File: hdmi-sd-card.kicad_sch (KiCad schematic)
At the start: 33 parts, among them J4 HDMI-A_WE_685119134923, J5 MicroSD_693071020811, U10 TPD4E05U06QDQARQ1, U11 TPD4E05U06QDQARQ1, U12 TPD4E05U06QDQARQ1, U14 TPD4E05U06QDQARQ1

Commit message: [#65754] Rename project
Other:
- title: SO-DIMM DDR5 Tester -> RDIMM DDR5 Tester

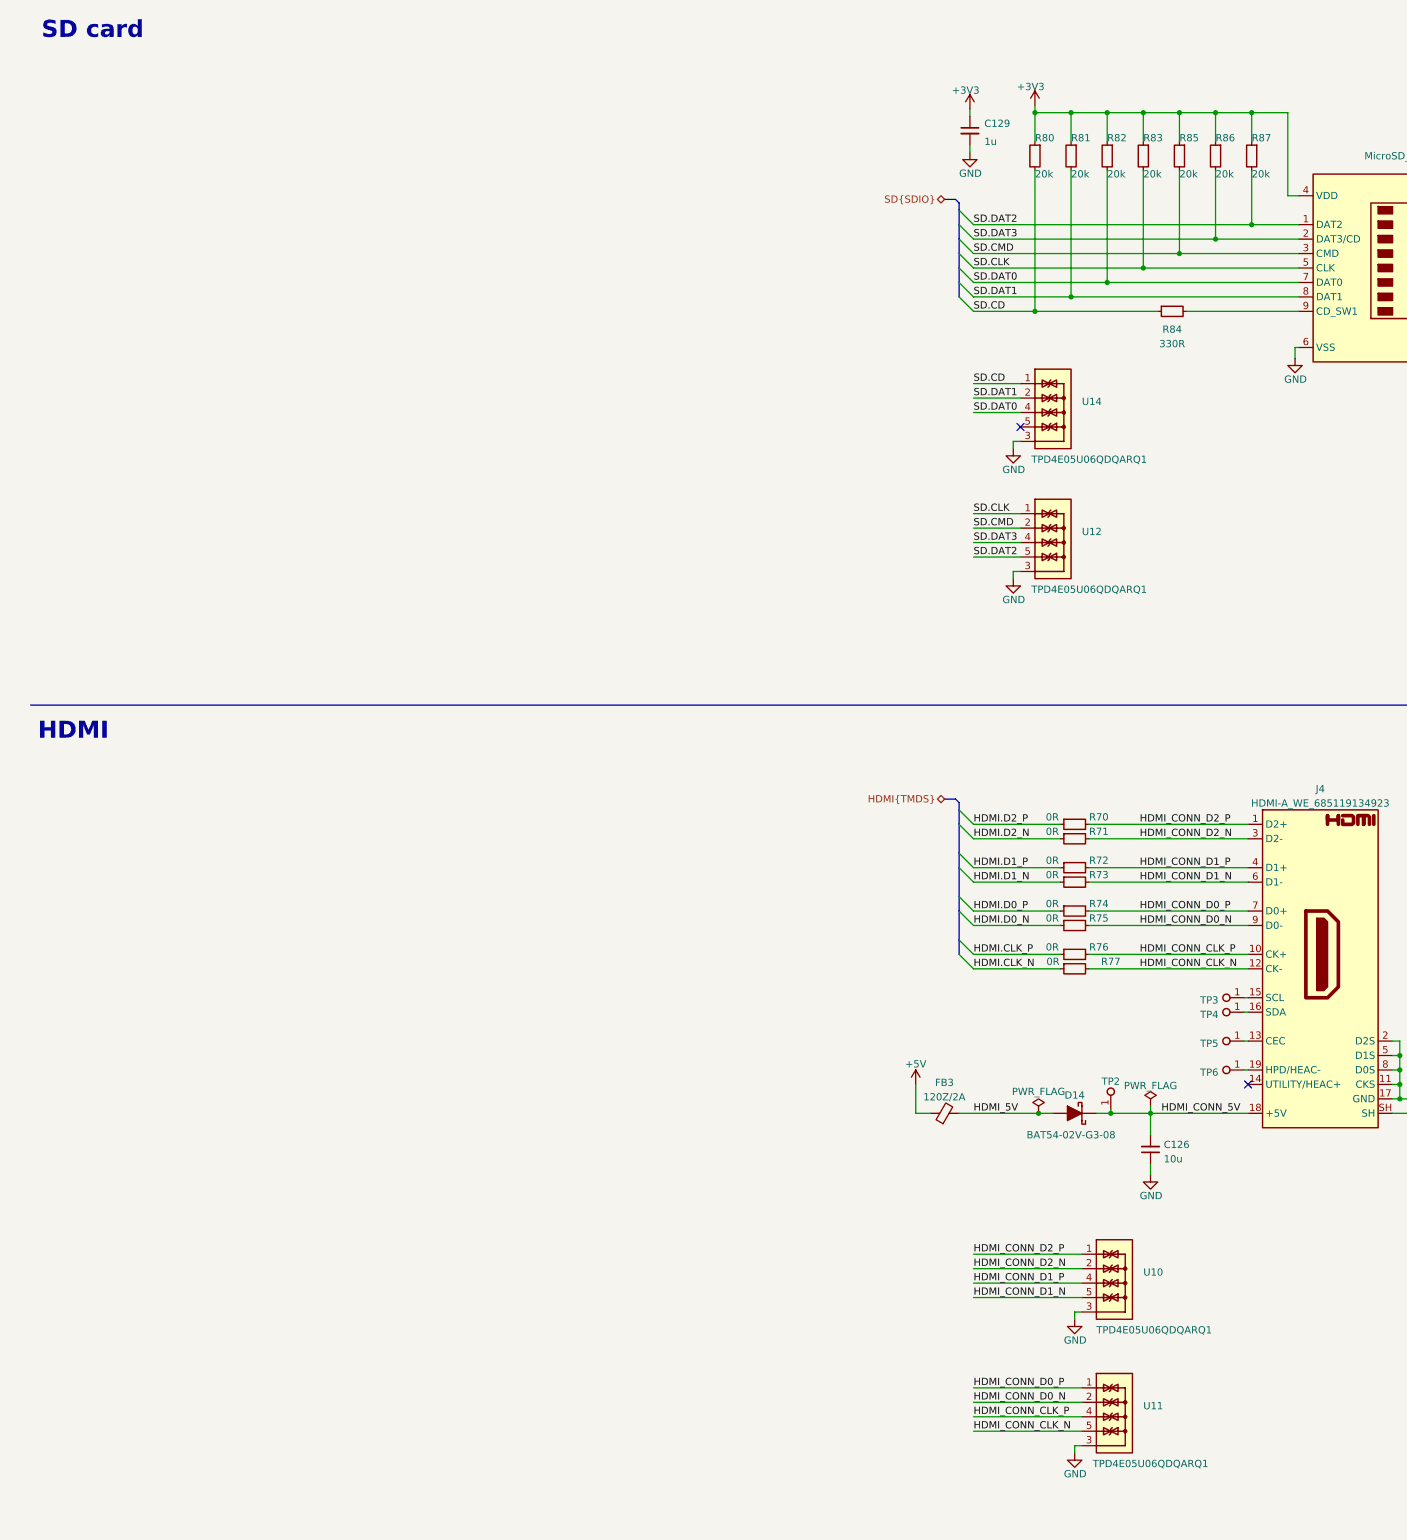
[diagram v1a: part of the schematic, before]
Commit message: [#66727] Finish connecting HDMI driver. Add SD card logic level converter. Add SD 3.0 support
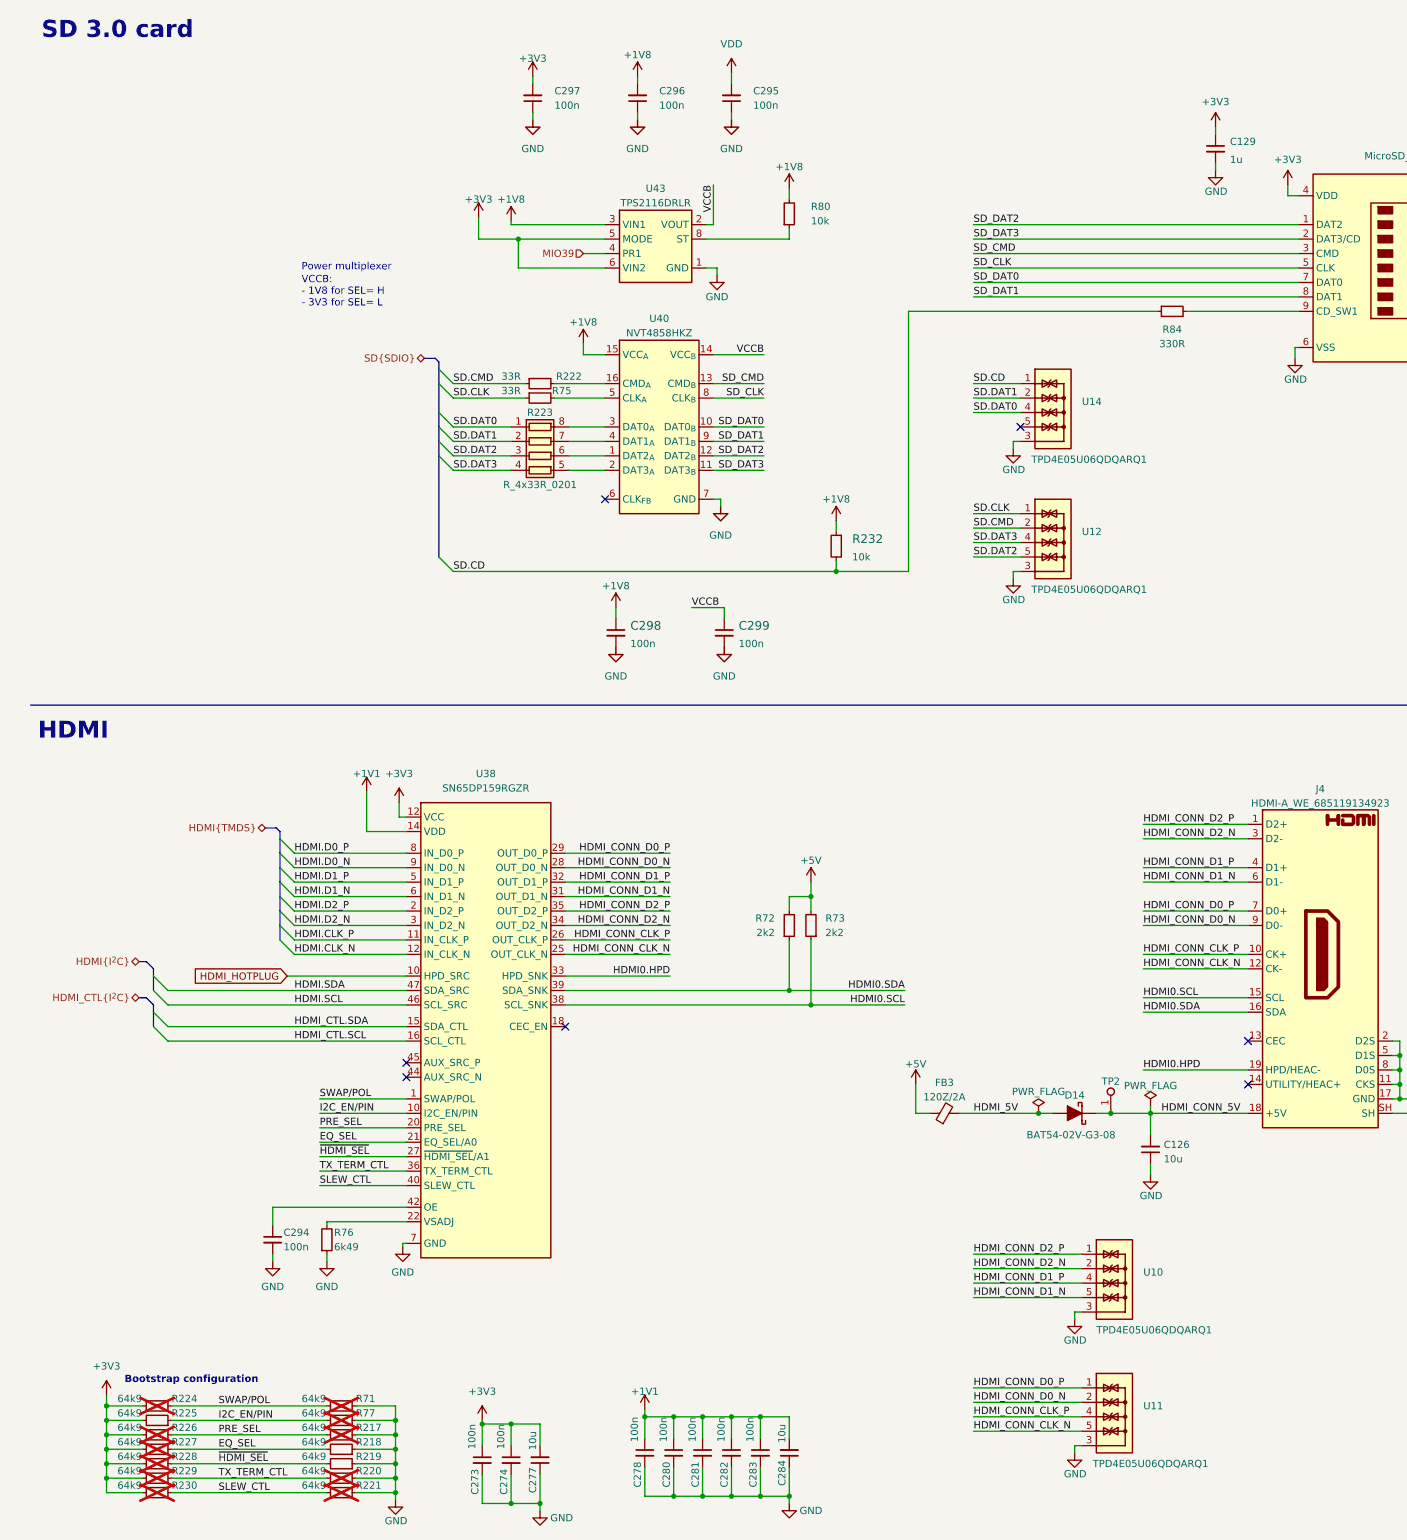
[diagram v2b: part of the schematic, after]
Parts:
- removed R70, R71, R72, R73, R74, R75, R76, R77: R_0R_0402, antmicro-footprints:R_0402_1005Metric, symbol antmicroResistors0402:R_0R_0402
- removed R80, R81, R82, R83, R85, R86, R87: R_20k_0402, antmicro-footprints:R_0402_1005Metric, symbol antmicroResistors0402:R_20k_0402
- removed TP3, TP4, TP5, TP6: TP_1mm_SMD, antmicro-footprints:TP_SMD_1mm, symbol antmicroTestPoints:TP_1mm_SMD
- added C273, C274, C278, C280, C281, C282, C283, C294, C295, C296, C297: C_100n_0402, antmicro-footprints:C_0402_1005Metric, symbol antmicroCapacitors0402:C_100n_0402
- added C277, C284: C_10u_10V_0402, antmicro-footprints:C_0402_1005Metric, symbol antmicroCapacitors0402:C_10u_10V_0402
- added C298, C299: C_100n_0402, kria-k26-devboard-footprints:C_0402_1005Metric, symbol kria-k26-devboard:C_100n_0402
- added R217, R218, R219, R220, R221, R224, R225, R226, R227, R228, R229, R230, R71, R77: R_64k9_0402, antmicro-footprints:R_0402_1005Metric, symbol antmicroResistors0402:R_64k9_0402
- added R222, R75: R_33R_0402, antmicro-footprints:R_0402_1005Metric, symbol antmicroResistors0402:R_33R_0402
- added R223: R_4x33R_0201_array, antmicro-footprints:R_Array_4x0201_Panasonic_EXB18V, symbol antmicroResistorNetworksArrays:R_4x33R_0201_array
- added R232: R_10k_0402, kria-k26-devboard-footprints:R_0402_1005Metric, symbol kria-k26-devboard:R_10k_0402
- added R72, R73: R_2k2_0402, antmicro-footprints:R_0402_1005Metric, symbol antmicroResistors0402:R_2k2_0402
- added R76: R_6k49_0402, antmicro-footprints:R_0402_1005Metric, symbol antmicroResistors0402:R_6k49_0402
- added R80: R_10k_0402, antmicro-footprints:R_0402_1005Metric, symbol antmicroResistors0402:R_10k_0402
- added U38: SN65DP159RGZR, antmicro-footprints:VQFN-48_7x7mm_P0.5mm_EP4.1x4.1mm, symbol antmicroInterfaceDriversReceiversTransceivers:SN65DP159RGZR
- added U40: NVT4858_XQFN, antmicro-footprints:SOT1161-2, symbol antmicroLogicTranslatorsLevelShifters:NVT4858_XQFN
- added U43: TPS2116DRLR, antmicro-footprints:SOT-583, symbol antmicroPMICPowerDistributionSwitchesLoadDrivers:TPS2116DRLR
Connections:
- net +3V3: now also C273.1, C274.1, C277.2, C297.2, R224.2, R225.2, R226.2, R227.2, R228.2, R229.2, R230.2, U38.12 (VCC), U38.43 (VCC), U43.5 (MODE), U43.6 (VIN2)
- net +5V: now also R72.2, R73.2
- net GND: now also C273.2, C274.2, C277.1, C278.2, C280.2, C281.2, C282.2, C283.2, C284.1, C294.2, C295.1, C296.1, C297.1, C298.2, C299.2, R217.1, R218.1, R219.1, R220.1, R221.1, R71.1, R76.1, R77.1, U38.19 (GND), U38.30 (GND), U38.41 (GND), U38.49 (GND), U38.7 (GND), U40.7 (GND), U43.1 (GND)
- net HDMI.CLK_N: now also U38.12 (VCC)
- net HDMI.CLK_P: now also U38.11 (IN_CLK_P)
- net HDMI.D0_N: now also U38.9 (IN_D0_N)
- net HDMI.D0_P: now also U38.8 (IN_D0_P)
- net HDMI.D1_N: now also U38.6 (IN_D1_N)
- net HDMI.D1_P: now also U38.5 (IN_D1_P)
- net HDMI.D2_N: now also U38.3 (IN_D2_N)
- net HDMI.D2_P: now also U38.2 (IN_D2_P)
- net HDMI_CONN_CLK_N: now also U38.25 (OUT_CLK_N)
- net HDMI_CONN_CLK_P: now also U38.26 (OUT_CLK_P)
- net HDMI_CONN_D0_N: now also U38.28 (OUT_D0_N)
- net HDMI_CONN_D0_P: now also U38.29 (OUT_D0_P)
- net HDMI_CONN_D1_N: now also U38.31 (OUT_D1_N)
- net HDMI_CONN_D1_P: now also U38.32 (OUT_D1_P)
- net HDMI_CONN_D2_N: now also U38.34 (OUT_D2_N)
- net HDMI_CONN_D2_P: now also U38.35 (OUT_D2_P)
- net SD.CD: now also R232.2
- net SD.CLK: now also R75.1; no longer J5.5 (CLK)
- net SD.CMD: now also R222.1; no longer J5.3 (CMD)
- net SD.DAT0: now also R223.1 (R1.1); no longer J5.7 (DAT0)
- net SD.DAT1: now also R223.2 (R2.1); no longer J5.8 (DAT1)
- net SD.DAT2: now also R223.3 (R3.1); no longer J5.1 (DAT2)
- net SD.DAT3: now also R223.4 (R4.1); no longer J5.2 (DAT3/CD)
- net HDMI0.SCL: now reaches J4.15 (SCL)
- net HDMI0.SCL: now also R73.1, U38.38 (SCL_SNK)
- net HDMI0.SDA: now reaches J4.16 (SDA)
- net HDMI0.SDA: now also R72.1, U38.39 (SDA_SNK)
- net HDMI0.HPD: now reaches J4.19 (HPD/HEAC-)
- net HDMI0.HPD: now also U38.33 (HPD_SNK)
- new net: R76.2, U38.22 (VSADJ)
- new net: R223.6 (R3.2), U40.1 (DAT2_{A})
- new net: R222.2, U40.16 (CMD_{A})
- new net: R223.5 (R4.2), U40.2 (DAT3_{A})
- new net: R223.8 (R1.2), U40.3 (DAT0_{A})
- new net: R223.7 (R2.2), U40.4 (DAT1_{A})
- new net: R75.2, U40.5 (CLK_{A})
- new net: C294.1, U38.42 (OE)
- new net: R80.1, U43.8 (ST)
- new net +1V1: C278.1, C280.1, C281.1, C282.1, C283.1, C284.2, C295.2, U38.14 (VDD), U38.23 (VDD), U38.24 (VDD), U38.37 (VDD), U38.48 (VDD)
- new net +1V8: C296.2, C298.1, R232.1, R80.2, U40.15 (VCC_{A}), U43.3 (VIN1)
- new net EQ_SEL: R218.2, R227.1, U38.21 (EQ_SEL/A0)
- new net HDMI.SCL: U38.46 (SCL_SRC)
- new net HDMI.SDA: U38.47 (SDA_SRC)
- new net HDMI_CTL.SCL: U38.16 (SCL_CTL)
- new net HDMI_CTL.SDA: U38.15 (SDA_CTL)
- new net HDMI_HOTPLUG: U38.10 (I2C_EN/PIN)
- new net I2C_EN/PIN: R225.1, R77.2, U38.10 (I2C_EN/PIN)
- new net MIO39: U43.4 (PR1)
- new net PRE_SEL: R217.2, R226.1, U38.20 (PRE_SEL)
- new net SD_CLK: J5.5 (CLK), U40.8 (CLK_{B})
- new net SD_CMD: J5.3 (CMD), U40.13 (CMD_{B})
- new net SD_DAT0: J5.7 (DAT0), U40.10 (DAT0_{B})
- new net SD_DAT1: J5.8 (DAT1), U40.9 (DAT1_{B})
- new net SD_DAT2: J5.1 (DAT2), U40.12 (DAT2_{B})
- new net SD_DAT3: J5.2 (DAT3/CD), U40.11 (DAT3_{B})
- new net SLEW_CTL: R221.2, R230.1, U38.40 (SLEW_CTL)
- new net SWAP/POL: R224.1, R71.2, U38.1 (SWAP/POL)
- new net TX_TERM_CTL: R220.2, R229.1, U38.36 (TX_TERM_CTL)
- new net VCCB: C299.1, U40.14 (VCC_{B}), U43.2 (VOUT), U43.7 (VOUT)
- new net ~{HDMI_SEL}: R219.2, R228.1, U38.27 (~{HDMI_SEL}/A1)
- no-connect marks 2 -> 7
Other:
- note added: "Bootstrap configuration"
- note added: "Power multiplexer"
- note added: "SD 3.0 card"
- note added: "VCCB: - 1V8 for SEL= H - 3V3 for SEL= L"
- note removed: "SD card"
- moved on the sheet: C129

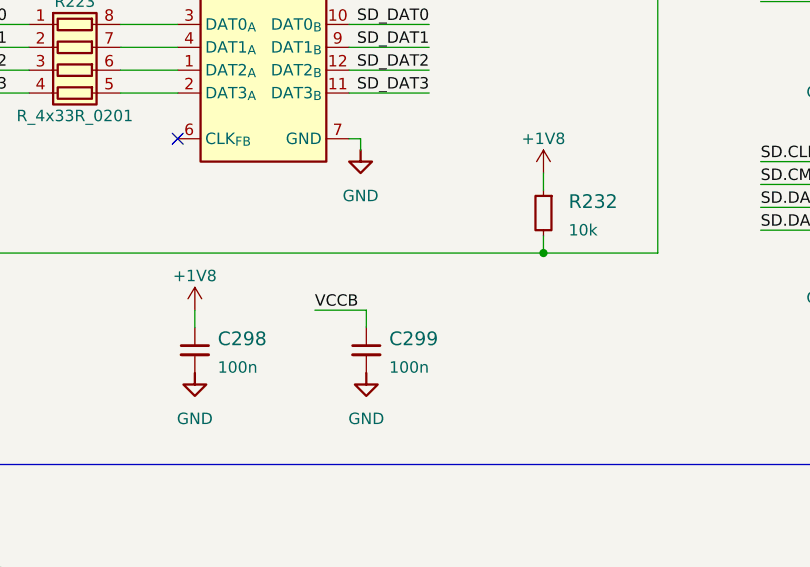
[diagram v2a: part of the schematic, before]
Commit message: [#66727] Update legacy footprints
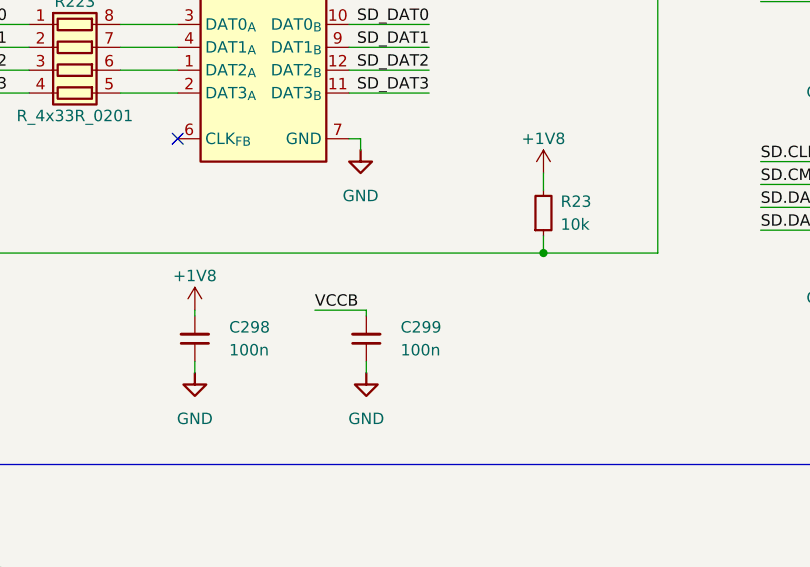
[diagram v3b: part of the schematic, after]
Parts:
- removed C298, C299: C_100n_0402, kria-k26-devboard-footprints:C_0402_1005Metric, symbol kria-k26-devboard:C_100n_0402
- removed R232: R_10k_0402, kria-k26-devboard-footprints:R_0402_1005Metric, symbol kria-k26-devboard:R_10k_0402
- added C298, C299: C_100n_0402, antmicro-footprints:C_0402_1005Metric, symbol antmicroCapacitors0402:C_100n_0402
- added R23: R_10k_0402, antmicro-footprints:R_0402_1005Metric, symbol Resistors0402:R_10k_0402
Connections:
- net +1V8: now also C298.2, R23.2
- net GND: now also C298.1, C299.1
- net SD.CD: now also R23.1
- net VCCB: now also C299.2

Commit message: [#66311] Start connecting HDMI RX to GTH226 quad
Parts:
- added C300: C_100n_0402, antmicro-footprints:C_0402_1005Metric, symbol antmicroCapacitors0402:C_100n_0402
- added C301: C_10u_6.3V_0402, antmicro-footprints:C_0402_1005Metric, symbol antmicroCapacitors0402:C_10u_6.3V_0402
- added FB7: FB_120Z_1.3A_Murata-BLM15PD_0402, antmicro-footprints:FB_0402_1005Metric, symbol antmicroFerriteBeadsandChips:FB_120Z_1.3A_Murata-BLM15PD_0402
- added J11: I-PEX_CABLINE-VS_1x20_20455-A20E-76, antmicro-footprints:I-PEX_CABLINE-VS_1x20_20455-A20E-76, symbol antmicroWire2BoardConnectors:I-PEX_CABLINE-VS_1x20_20455-A20E-76
- added L10, L3, L4, L5, L6, L7, L8, L9: L_20n_0.35A_0402, antmicro-footprints:L_0402_1005Metric, symbol antmicroFixedInductors:L_20n_0.35A_0402
- added R24, R28, R29, R30, R31, R32, R33, R34: R_49k9_0402, antmicro-footprints:R_0402_1005Metric, symbol antmicroResistors0402:R_49k9_0402
- added U37, U41: TPD4E05U06QDQARQ1, antmicro-footprints:USON-10_2.5x1mm_P0.5mm, symbol antmicroTVSDiodes:TPD4E05U06QDQARQ1
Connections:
- net +3V3: now also FB7.1
- net GND: now also C300.1, C301.1, J11.11, J11.17, J11.2, J11.5, J11.8, J11.SH, U37.3, U37.8, U41.3, U41.8
- net HDMI0.HPD: now also J11.19
- net HDMI0.SCL: now also J11.15
- net HDMI0.SDA: now also J11.16
- net HDMI.CLK_N renamed HDMI_OUT.CLK_N
- net HDMI.CLK_P renamed HDMI_OUT.CLK_P
- net HDMI.D0_N renamed HDMI_OUT.D0_N
- net HDMI.D0_P renamed HDMI_OUT.D0_P
- net HDMI.D1_N renamed HDMI_OUT.D1_N
- net HDMI.D1_P renamed HDMI_OUT.D1_P
- net HDMI.D2_N renamed HDMI_OUT.D2_N
- net HDMI.D2_P renamed HDMI_OUT.D2_P
- net HDMI_CONN_CLK_N renamed HDMI_OUT_CONN_CLK_N
- net HDMI_CONN_CLK_P renamed HDMI_OUT_CONN_CLK_P
- net HDMI_CONN_D0_N renamed HDMI_OUT_CONN_D0_N
- net HDMI_CONN_D0_P renamed HDMI_OUT_CONN_D0_P
- net HDMI_CONN_D1_N renamed HDMI_OUT_CONN_D1_N
- net HDMI_CONN_D1_P renamed HDMI_OUT_CONN_D1_P
- net HDMI_CONN_D2_N renamed HDMI_OUT_CONN_D2_N
- net HDMI_CONN_D2_P renamed HDMI_OUT_CONN_D2_P
- new net: C300.2, C301.2, FB7.2, R24.2, R28.2, R29.2, R30.2, R31.2, R32.2, R33.2, R34.2
- new net: L6.2, R30.1
- new net: L7.2, R31.1
- new net: L8.2, R32.1
- new net: L9.2, R33.1
- new net: L3.2, R24.1
- new net: L10.2, R34.1
- new net: L5.2, R29.1
- new net: L4.2, R28.1
- new net HDMI_IN.CLK_N: J11.12, L7.1
- new net HDMI_IN.CLK_P: J11.10, L8.1
- new net HDMI_IN.D0_N: J11.9, L9.1
- new net HDMI_IN.D0_P: J11.7, L10.1
- new net HDMI_IN.D1_N: J11.6, L5.1
- new net HDMI_IN.D1_P: J11.4, L3.1
- new net HDMI_IN.D2_N: J11.3, L4.1
- new net HDMI_IN.D2_P: J11.1, L6.1
- new net HDMI_IN_CONN_CLK_N: U41.5, U41.6
- new net HDMI_IN_CONN_CLK_P: U41.4, U41.7
- new net HDMI_IN_CONN_D0_N: U41.2, U41.9
- new net HDMI_IN_CONN_D0_P: U41.1, U41.10
- new net HDMI_IN_CONN_D1_N: U37.5, U37.6
- new net HDMI_IN_CONN_D1_P: U37.4, U37.7
- new net HDMI_IN_CONN_D2_N: U37.2, U37.9
- new net HDMI_IN_CONN_D2_P: U37.1, U37.10
- no-connect marks 7 -> 10
